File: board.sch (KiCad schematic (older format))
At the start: 50 parts, among them J1 LASER, J10 Mode, J11 Y, J12 12V, J13 Y, J14 X, J15 12V-36V, J16 CNC_OUT2, J2 Pololu_Breakout_A4988, J3 V_LASER, J4 Pololu_Breakout_A4988, J5 Z, J6 Pololu_Breakout_A4988, J7 12-36V, J8 Arduino_Nano, J9 Misc, K1 SRD-12VDC-SL-C, Q1 Y2, Q2 WJ0625A, T1 Logo_Open_Hardware_Small, U1 PC817, U2 XL4015E1

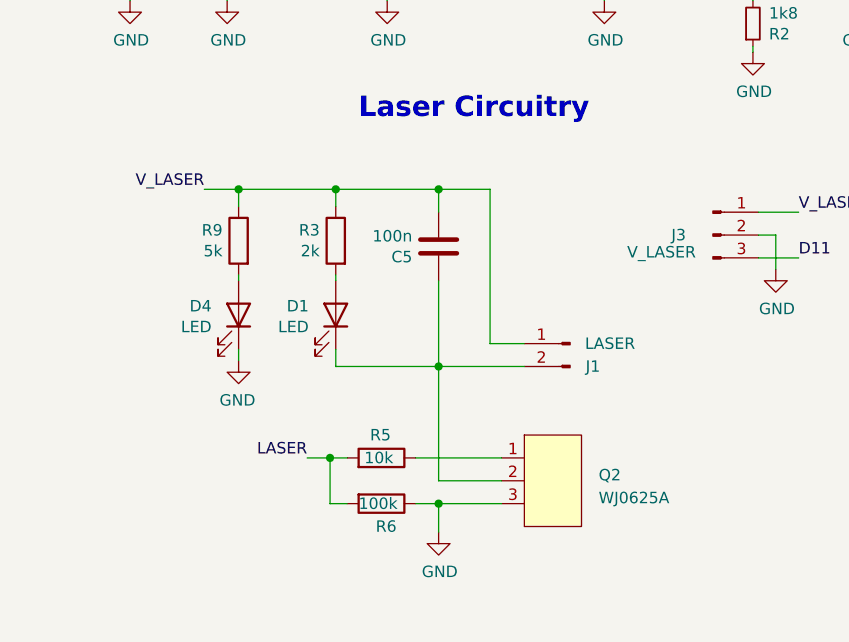
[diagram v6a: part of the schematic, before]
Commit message: Fix n-mosfet symbol/footprint and improve circuit
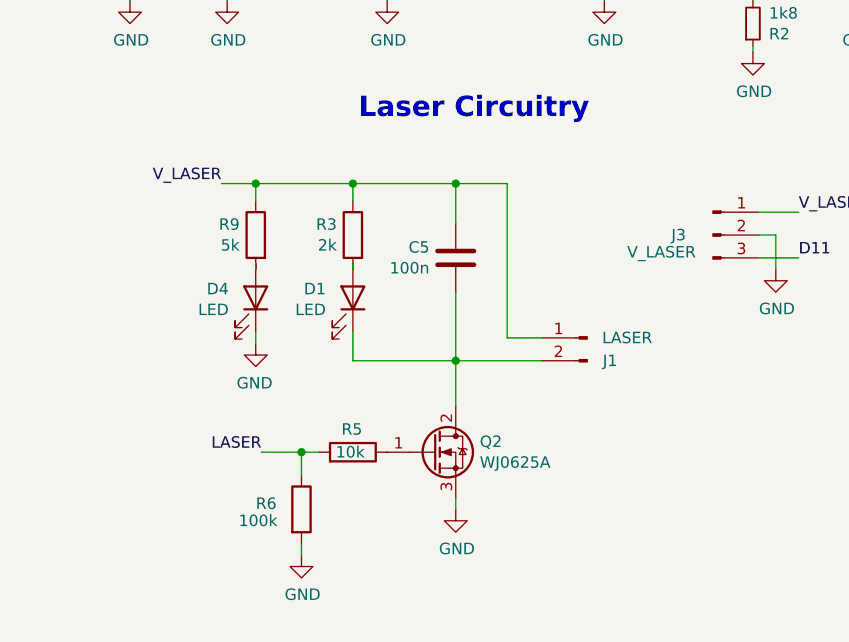
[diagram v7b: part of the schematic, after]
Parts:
- removed Q2: WJ0625A, Package_TO_SOT_SMD:TO-252-3_TabPin2, symbol Developower:WJ0625A
- added Q2: WJ0625A, Package_TO_SOT_SMD:TO-252-2, symbol Device:Q_NMOS_GDS
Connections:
- net GND: now also R6.2, Q2.3 (S); no longer R6.1
- net LASER: now also R6.1; no longer R6.2
- net V_LASER: now also C5.1; no longer C5.2
- net at D1.1 (K), J1.2 (Pin_2): now also C5.2, Q2.2 (D); no longer C5.1
- net at R5.1: now also Q2.1 (G)
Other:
- moved on the sheet: C5, D1, D4, J1, R3, R5, R6, R9
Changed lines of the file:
@@
 L Connector:Conn_01x02_Male J1
 U 1 1 5E0121DB
-P 3350 6500
-F 0 "J1" H 3250 6400 50  0000 C CNN
-F 1 "LASER" H 3175 6500 50  0000 C CNN
-F 2 "Developower:JST_S2B-XH-A(LF)(SN)" H 3350 6500 50  0001 C CNN
-F 3 "~" H 3350 6500 50  0001 C CNN
-	1    3350 6500
+P 3425 6475
+F 0 "J1" H 3325 6375 50  0000 C CNN
+F 1 "LASER" H 3250 6475 50  0000 C CNN
+F 2 "Developower:JST_S2B-XH-A(LF)(SN)" H 3425 6475 50  0001 C CNN
+F 3 "~" H 3425 6475 50  0001 C CNN
+	1    3425 6475
 	-1   0    0    -1
 $EndComp
@@
 L Device:C C5
 U 1 1 6080D262
-P 2775 6075
-F 0 "C5" H 2890 6121 50  0000 L CNN
-F 1 "100n" H 2890 6030 50  0000 L CNN
-F 2 "Capacitor_SMD:C_1206_3216Metric" H 2813 5925 50  0001 C CNN
-F 3 "~" H 2775 6075 50  0001 C CNN
-	1    2775 6075
-	-1   0    0    1
+P 2850 6125
+F 0 "C5" H 2965 6171 50  0000 L CNN
+F 1 "100n" H 2965 6080 50  0000 L CNN
+F 2 "Capacitor_SMD:C_1206_3216Metric" H 2888 5975 50  0001 C CNN
+F 3 "~" H 2850 6125 50  0001 C CNN
+	1    2850 6125
+	-1   0    0    -1
 $EndComp
 $Comp
@@
 F 3 "http://www.soselectronic.cz/a_info/resource/d/pc817.pdf" H 7725 4350 50  0001 L CNN
 	1    7725 4350
-	1    0    0    -1
-$EndComp
-$Comp
-L Developower:WJ0625A Q2
-U 1 1 608700DB
-P 3200 6850
-F 0 "Q2" H 3475 6625 50  0000 L CNN
-F 1 "WJ0625A" H 3475 6525 50  0000 L CNN
-F 2 "Package_TO_SOT_SMD:TO-252-3_TabPin2" H 3200 6850 50  0001 C CNN
-F 3 "" H 3200 6850 50  0001 C CNN
-	1    3200 6850
 	1    0    0    -1
 $EndComp
@@
 D10
 Wire Wire Line
-	2775 6600 2775 6225
+	2850 6575 2850 6275
 Wire Wire Line
 	6375 2425 6400 2425
@@
 L Device:R R6
 U 1 1 6081D716
-P 2525 7200
-F 0 "R6" V 2625 7175 50  0000 L CNN
-F 1 "100k" V 2525 7100 50  0000 L CNN
-F 2 "Resistor_SMD:R_0805_2012Metric" V 2455 7200 50  0001 C CNN
-F 3 "~" H 2525 7200 50  0001 C CNN
-	1    2525 7200
-	0    1    1    0
+P 2175 7225
+F 0 "R6" H 1975 7250 50  0000 L CNN
+F 1 "100k" H 1900 7175 50  0000 L CNN
+F 2 "Resistor_SMD:R_0805_2012Metric" V 2105 7225 50  0001 C CNN
+F 3 "~" H 2175 7225 50  0001 C CNN
+	1    2175 7225
+	1    0    0    -1
 $EndComp
 $Comp
 L Device:R R5
 U 1 1 6081D2EA
-P 2525 7000
-F 0 "R5" V 2625 6950 50  0000 L CNN
-F 1 "10k" V 2525 6925 50  0000 L CNN
-F 2 "Resistor_SMD:R_0805_2012Metric" V 2455 7000 50  0001 C CNN
-F 3 "~" H 2525 7000 50  0001 C CNN
-	1    2525 7000
+P 2400 6975
+F 0 "R5" V 2500 6925 50  0000 L CNN
+F 1 "10k" V 2400 6900 50  0000 L CNN
+F 2 "Resistor_SMD:R_0805_2012Metric" V 2330 6975 50  0001 C CNN
+F 3 "~" H 2400 6975 50  0001 C CNN
+	1    2400 6975
 	0    1    -1   0
 $EndComp
@@
 $EndComp
 Wire Wire Line
-	2375 7200 2300 7200
-Wire Wire Line
-	2300 7200 2300 7000
-Wire Wire Line
-	2300 7000 2375 7000
-Wire Wire Line
-	2675 7000 3050 7000
-Wire Wire Line
-	2675 7200 2775 7200
-Wire Wire Line
-	2300 7000 2200 7000
-Connection ~ 2300 7000
-Text Label 2200 7000 2    50   ~ 0
+	2175 7075 2175 6975
+Wire Wire Line
+	2175 6975 2250 6975
+Wire Wire Line
+	2175 6975 2000 6975
+Connection ~ 2175 6975
+Text Label 2000 6975 2    50   ~ 0
 LASER
 Text Label 3975 1675 0    50   ~ 0
@@
 Wire Wire Line
 	6950 4250 7075 4250
-Wire Wire Line
-	3050 7100 2775 7100
 Wire Wire Line
 	8300 5525 8300 5600
@@
 $EndComp
 Wire Wire Line
-	2775 6600 2775 7100
-Wire Wire Line
-	2775 6600 3150 6600
-Connection ~ 2775 6600
-Wire Wire Line
-	3150 6500 3000 6500
-Wire Wire Line
-	3000 6500 3000 5825
-Wire Wire Line
-	3000 5825 2775 5825
-Wire Wire Line
-	2775 5925 2775 5825
-Wire Wire Line
-	1900 5825 2325 5825
+	2850 6575 3225 6575
+Connection ~ 2850 6575
+Wire Wire Line
+	3225 6475 3075 6475
+Wire Wire Line
+	3075 6475 3075 5800
+Wire Wire Line
+	3075 5800 2850 5800
+Wire Wire Line
+	2850 5975 2850 5800
+Wire Wire Line
+	1975 5800 2400 5800
 $Comp
 L power:GND #PWR0131
 U 1 1 60F2778C
-P 1900 6575
-F 0 "#PWR0131" H 1900 6325 50  0001 C CNN
-F 1 "GND" H 1905 6402 50  0000 C CNN
-F 2 "" H 1900 6575 50  0001 C CNN
-F 3 "" H 1900 6575 50  0001 C CNN
-	1    1900 6575
+P 1975 6500
+F 0 "#PWR0131" H 1975 6250 50  0001 C CNN
+F 1 "GND" H 1980 6327 50  0000 C CNN
+F 2 "" H 1975 6500 50  0001 C CNN
+F 3 "" H 1975 6500 50  0001 C CNN
+	1    1975 6500
 	-1   0    0    -1
 $EndComp
@@
 L Device:LED D4
 U 1 1 6082DEF9
-P 1900 6375
-F 0 "D4" V 1939 6257 50  0000 R CNN
-F 1 "LED" V 1848 6257 50  0000 R CNN
-F 2 "LED_SMD:LED_0603_1608Metric" H 1900 6375 50  0001 C CNN
-F 3 "~" H 1900 6375 50  0001 C CNN
-	1    1900 6375
+P 1975 6300
+F 0 "D4" V 2014 6182 50  0000 R CNN
+F 1 "LED" V 1923 6182 50  0000 R CNN
+F 2 "LED_SMD:LED_0603_1608Metric" H 1975 6300 50  0001 C CNN
+F 3 "~" H 1975 6300 50  0001 C CNN
+	1    1975 6300
 	0    1    -1   0
 $EndComp
@@
 L Device:R R9
 U 1 1 6081DB87
-P 1900 6050
-F 0 "R9" H 1970 6096 50  0000 L CNN
-F 1 "5k" H 1970 6005 50  0000 L CNN
-F 2 "Resistor_SMD:R_0805_2012Metric" V 1830 6050 50  0001 C CNN
-F 3 "~" H 1900 6050 50  0001 C CNN
-	1    1900 6050
+P 1975 6025
+F 0 "R9" H 2045 6071 50  0000 L CNN
+F 1 "5k" H 2045 5980 50  0000 L CNN
+F 2 "Resistor_SMD:R_0805_2012Metric" V 1905 6025 50  0001 C CNN
+F 3 "~" H 1975 6025 50  0001 C CNN
+	1    1975 6025
 	-1   0    0    -1
 $EndComp
@@
 L Device:LED D1
 U 1 1 6082D799
-P 2325 6375
-F 0 "D1" V 2364 6257 50  0000 R CNN
-F 1 "LED" V 2273 6257 50  0000 R CNN
-F 2 "LED_SMD:LED_0603_1608Metric" H 2325 6375 50  0001 C CNN
-F 3 "~" H 2325 6375 50  0001 C CNN
-	1    2325 6375
+P 2400 6300
+F 0 "D1" V 2439 6182 50  0000 R CNN
+F 1 "LED" V 2348 6182 50  0000 R CNN
+F 2 "LED_SMD:LED_0603_1608Metric" H 2400 6300 50  0001 C CNN
+F 3 "~" H 2400 6300 50  0001 C CNN
+	1    2400 6300
 	0    1    -1   0
 $EndComp
 Wire Wire Line
-	2325 5825 2325 5900
+	2400 5800 2400 5875
 $Comp
 L Device:R R3
 U 1 1 6081DF8D
-P 2325 6050
-F 0 "R3" H 2395 6096 50  0000 L CNN
-F 1 "2k" H 2395 6005 50  0000 L CNN
-F 2 "Resistor_SMD:R_0805_2012Metric" V 2255 6050 50  0001 C CNN
-F 3 "~" H 2325 6050 50  0001 C CNN
-	1    2325 6050
+P 2400 6025
+F 0 "R3" H 2470 6071 50  0000 L CNN
+F 1 "2k" H 2470 5980 50  0000 L CNN
+F 2 "Resistor_SMD:R_0805_2012Metric" V 2330 6025 50  0001 C CNN
+F 3 "~" H 2400 6025 50  0001 C CNN
+	1    2400 6025
 	-1   0    0    -1
 $EndComp
 Wire Wire Line
-	2775 6600 2325 6600
+	2850 6575 2400 6575
 Wire Wire Line
 	10425 4750 10350 4750
 Wire Wire Line
-	2325 5825 2775 5825
-Connection ~ 2325 5825
-Connection ~ 2775 5825
-Wire Wire Line
-	1900 6525 1900 6575
+	2400 5800 2850 5800
+Connection ~ 2400 5800
+Connection ~ 2850 5800
+Wire Wire Line
+	1975 6450 1975 6500
 Text Label 4350 5925 0    50   ~ 0
 V_LASER
@@
 V_STEP_MOT
 Wire Wire Line
-	1900 5900 1900 5825
+	1975 5875 1975 5800
 Wire Wire Line
 	6200 7225 6325 7225
@@
 Text Label 4925 4525 0    50   ~ 0
 V_LASER
-Text Label 1750 5825 2    50   ~ 0
+Text Label 1825 5800 2    50   ~ 0
 V_LASER
 Text Notes 8675 5150 0    89   ~ 18
@@
 Laser Circuitry
 Wire Wire Line
-	2325 6200 2325 6225
-Wire Wire Line
-	2325 6525 2325 6600
-Wire Wire Line
-	1900 6200 1900 6225
-Wire Wire Line
-	1750 5825 1900 5825
-Connection ~ 1900 5825
+	2400 6175 2400 6150
+Wire Wire Line
+	2400 6450 2400 6575
+Wire Wire Line
+	1975 6175 1975 6150
+Wire Wire Line
+	1825 5800 1975 5800
+Connection ~ 1975 5800
 $Comp
 L Device:C C6
@@
 	6325 7100 6325 7225
 Wire Wire Line
-	2775 7200 2775 7325
-Connection ~ 2775 7200
-Wire Wire Line
-	2775 7200 3050 7200
+	2850 7175 2850 7225
 $Comp
 L power:GND #PWR?
 U 1 1 60878EFA
-P 2775 7325
-F 0 "#PWR?" H 2775 7075 50  0001 C CNN
-F 1 "GND" H 2780 7152 50  0000 C CNN
-F 2 "" H 2775 7325 50  0001 C CNN
-F 3 "" H 2775 7325 50  0001 C CNN
-	1    2775 7325
-	1    0    0    -1
-$EndComp
+P 2850 7225
+F 0 "#PWR?" H 2850 6975 50  0001 C CNN
+F 1 "GND" H 2855 7052 50  0000 C CNN
+F 2 "" H 2850 7225 50  0001 C CNN
+F 3 "" H 2850 7225 50  0001 C CNN
+	1    2850 7225
+	1    0    0    -1
+$EndComp
+$Comp
+L Device:Q_NMOS_GDS Q2
+U 1 1 608627E4
+P 2750 6975
+F 0 "Q2" H 2955 7021 50  0000 L CNN
+F 1 "WJ0625A" H 2955 6930 50  0000 L CNN
+F 2 "Package_TO_SOT_SMD:TO-252-2" H 2950 7075 50  0001 C CNN
+F 3 "~" H 2750 6975 50  0001 C CNN
+	1    2750 6975
+	1    0    0    -1
+$EndComp
+Wire Wire Line
+	2175 7375 2175 7425
+$Comp
+L power:GND #PWR?
+U 1 1 609A49E2
+P 2175 7425
+F 0 "#PWR?" H 2175 7175 50  0001 C CNN
+F 1 "GND" H 2180 7252 50  0000 C CNN
+F 2 "" H 2175 7425 50  0001 C CNN
+F 3 "" H 2175 7425 50  0001 C CNN
+	1    2175 7425
+	1    0    0    -1
+$EndComp
+Wire Wire Line
+	2850 6775 2850 6575
 $EndSCHEMATC

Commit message: Update Q1
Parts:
- Q1: symbol Device:Q_NPN_BCE -> Device:Q_NMOS_GDS
- R3, R9: symbol Device:R -> Device:R_Small
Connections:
- net relay.p5: now also D5.2 (A), Q1.3 (S)
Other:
- moved on the sheet: C4, C5, C6, C7, C8, C9, D1, D2, D3, D4, D5, J1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
